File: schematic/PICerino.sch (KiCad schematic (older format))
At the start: 16 parts, among them J1 Conn_01x05, J2 Conn_01x03, J3 PJ-079BH, J4 Conn_01x03, J5 USB_B, J6 10046971-001LF, J7 Conn_01x32, U1 PIC18LF45K50-I_P

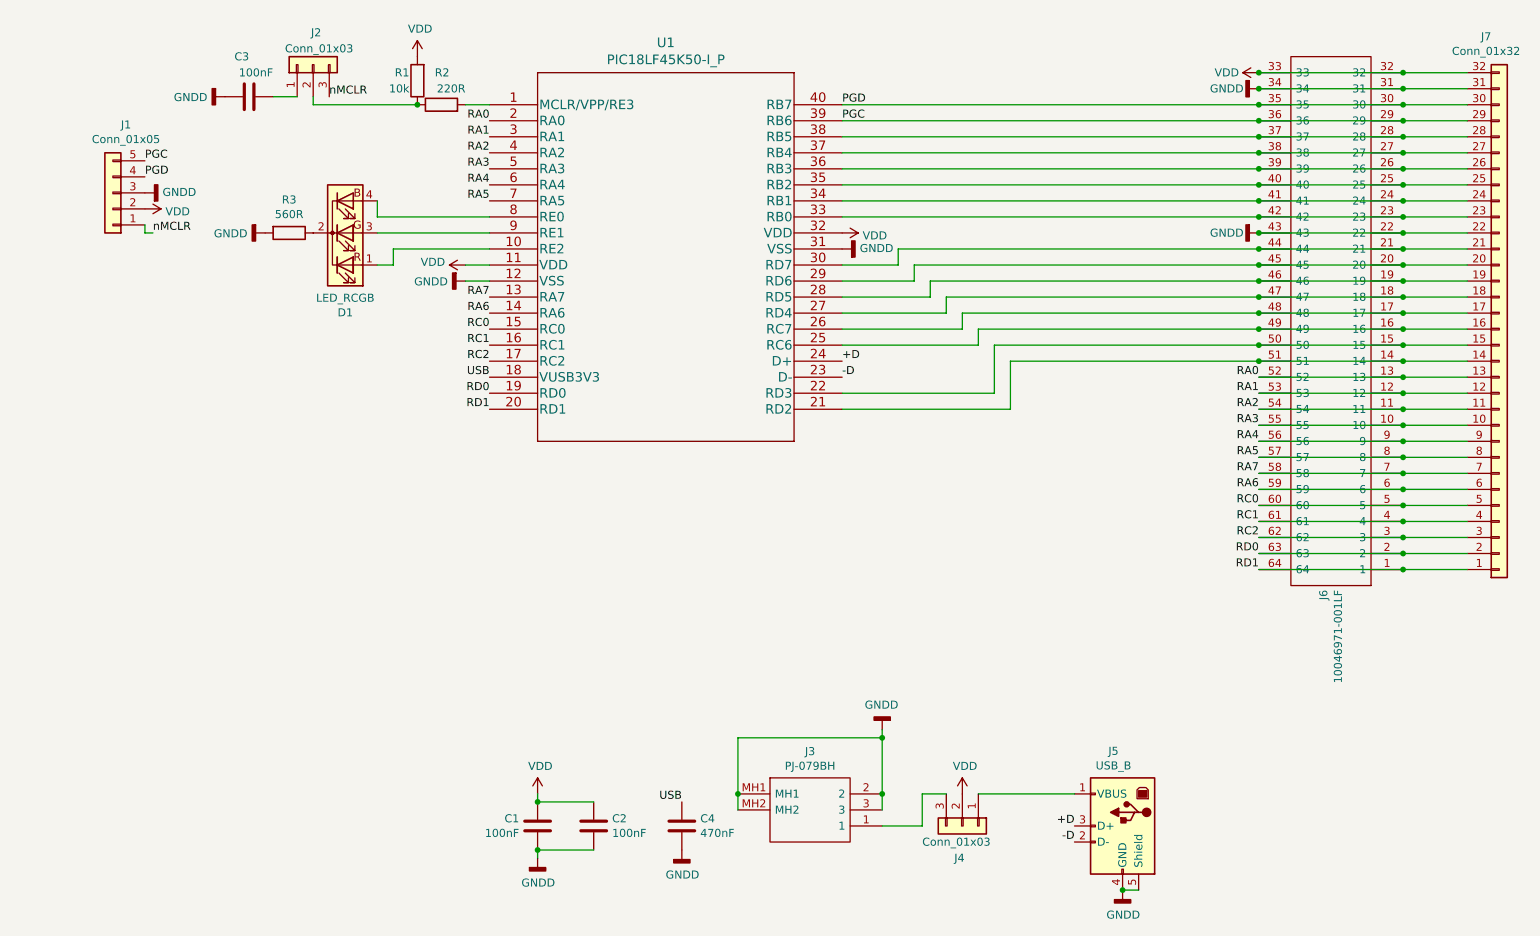
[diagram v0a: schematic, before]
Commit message: expanded picerino to have 3 slots instead of 1. allowing multiple devices to be used.
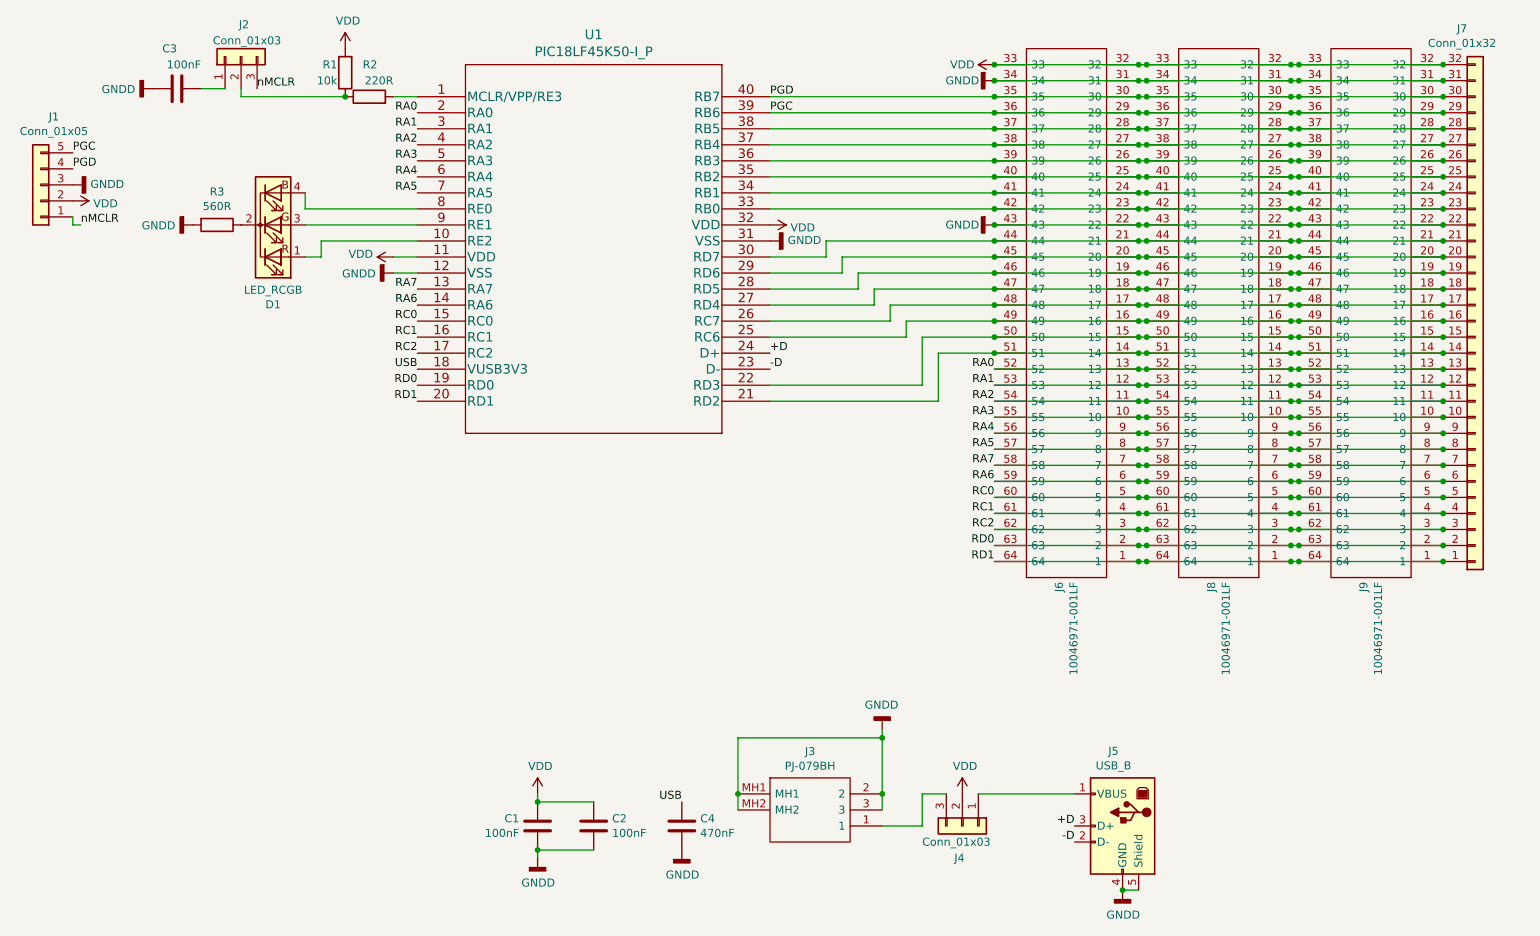
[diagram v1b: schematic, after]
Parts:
- added J8, J9: 10046971-001LF, 10046971-001LF:RHDR64W90P508X254_2X32_8786X929X1549P, symbol 10046971-001LF:10046971-001LF
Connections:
- net GNDD: now also J8.22, J8.31, J8.34, J8.43, J9.22, J9.31, J9.34, J9.43
- net PGC: now also J8.29, J8.36, J9.29, J9.36
- net PGD: now also J8.30, J8.35, J9.30, J9.35
- net RA0: now also J8.13, J8.52, J9.13, J9.52
- net RA1: now also J8.12, J8.53, J9.12, J9.53
- net RA2: now also J8.11, J8.54, J9.11, J9.54
- net RA3: now also J8.10, J8.55, J9.10, J9.55
- net RA4: now also J8.56, J8.9, J9.56, J9.9
- net RA5: now also J8.57, J8.8, J9.57, J9.8
- net RA6: now also J8.59, J8.6, J9.59, J9.6
- net RA7: now also J8.58, J8.7, J9.58, J9.7
- net RC0: now also J8.5, J8.60, J9.5, J9.60
- net RC1: now also J8.4, J8.61, J9.4, J9.61
- net RC2: now also J8.3, J8.62, J9.3, J9.62
- net RD0: now also J8.2, J8.63, J9.2, J9.63
- net RD1: now also J8.1, J8.64, J9.1, J9.64
- net VDD: now also J8.32, J8.33, J9.32, J9.33
- net at J6.14, J6.51, J7.14 (Pin_14)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: now also J8.14, J8.51, J9.14, J9.51
- net at J6.15, J6.50, J7.15 (Pin_15)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: now also J8.15, J8.50, J9.15, J9.50
- net at J6.16, J6.49, J7.16 (Pin_16)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: now also J8.16, J8.49, J9.16, J9.49
- net at J6.17, J6.48, J7.17 (Pin_17)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: now also J8.17, J8.48, J9.17, J9.48
- net at J6.18, J6.47, J7.18 (Pin_18)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: now also J8.18, J8.47, J9.18, J9.47
- net at J6.19, J6.46, J7.19 (Pin_19)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: now also J8.19, J8.46, J9.19, J9.46
- net at J6.20, J6.45, J7.20 (Pin_20)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: now also J8.20, J8.45, J9.20, J9.45
- net at J6.21, J6.44, J7.21 (Pin_21)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: now also J8.21, J8.44, J9.21, J9.44
- net at J6.23, J6.42, J7.23 (Pin_23)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: now also J8.23, J8.42, J9.23, J9.42
- net at J6.24, J6.41, J7.24 (Pin_24)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: now also J8.24, J8.41, J9.24, J9.41
- net at J6.25, J6.40, J7.25 (Pin_25)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: now also J8.25, J8.40, J9.25, J9.40
- net at J6.26, J6.39, J7.26 (Pin_26)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: now also J8.26, J8.39, J9.26, J9.39
- net at J6.27, J6.38, J7.27 (Pin_27)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: now also J8.27, J8.38, J9.27, J9.38
- net at J6.28, J6.37, J7.28 (Pin_28)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: now also J8.28, J8.37, J9.28, J9.37
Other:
- moved on the sheet: C3, D1, J1, J2, J6, J7, R1, R2, R3, U1
